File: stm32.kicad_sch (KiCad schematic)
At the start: 0 parts

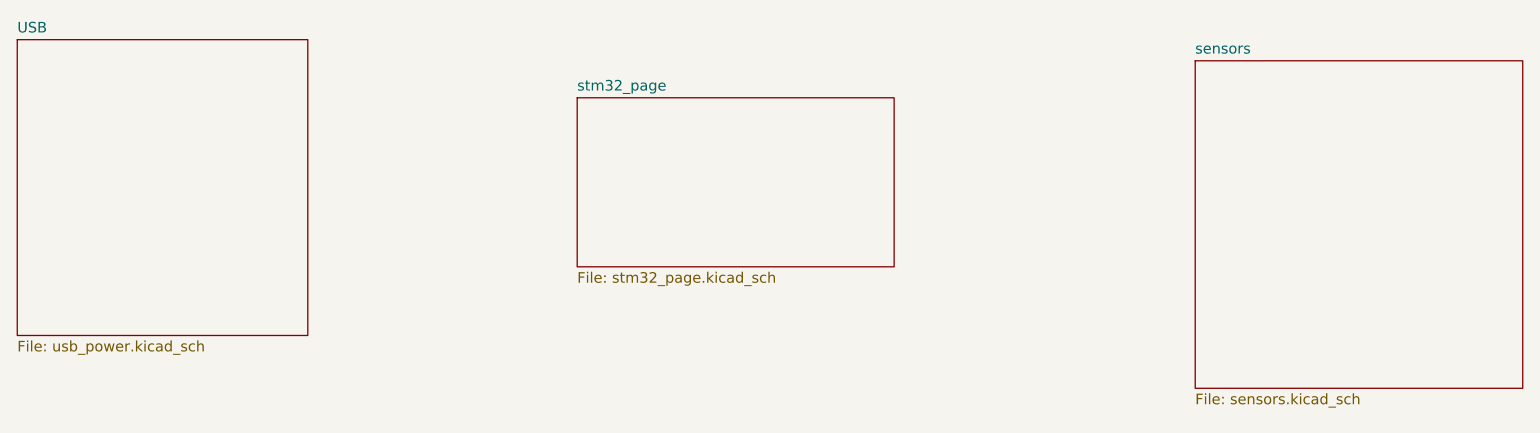
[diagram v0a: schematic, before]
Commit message: Finished schematic need to check , before layout
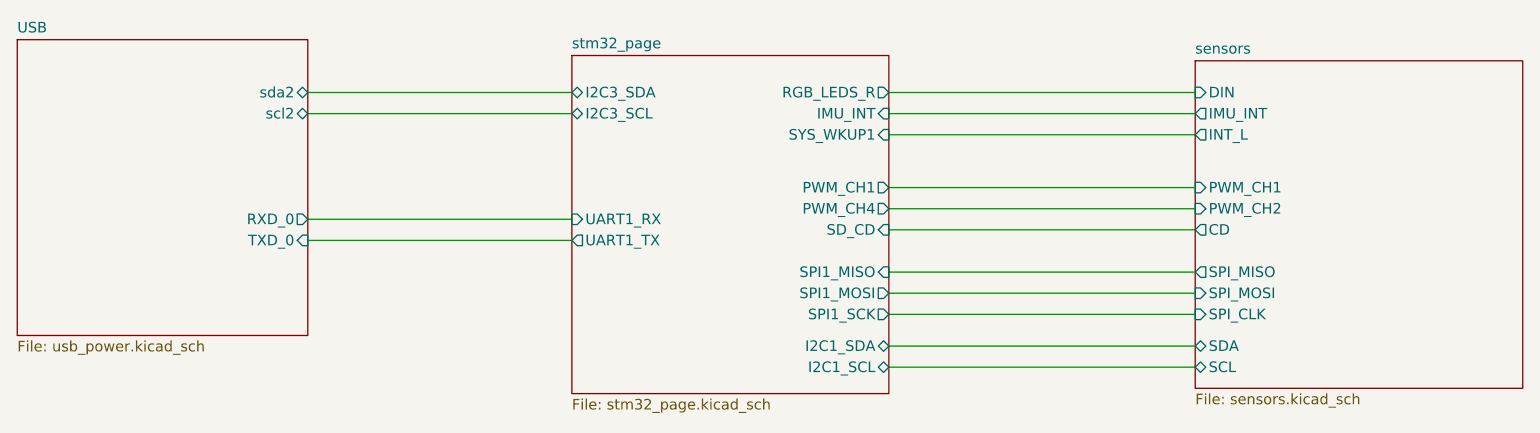
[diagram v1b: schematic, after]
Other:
- sheet USB ports: added RXD_0, TXD_0, scl2, sda2; removed none
- sheet sensors ports: added CD, DIN, IMU_INT, INT_L, PWM_CH1, PWM_CH2, SCL, SDA, SPI_CLK, SPI_MISO, SPI_MOSI; removed none
- sheet stm32_page ports: added I2C1_SCL, I2C1_SDA, I2C3_SCL, I2C3_SDA, IMU_INT, PWM_CH1, PWM_CH4, RGB_LEDS_R, SD_CD, SPI1_MISO, SPI1_MOSI, SPI1_SCK, SYS_WKUP1, UART1_RX, UART1_TX; removed none

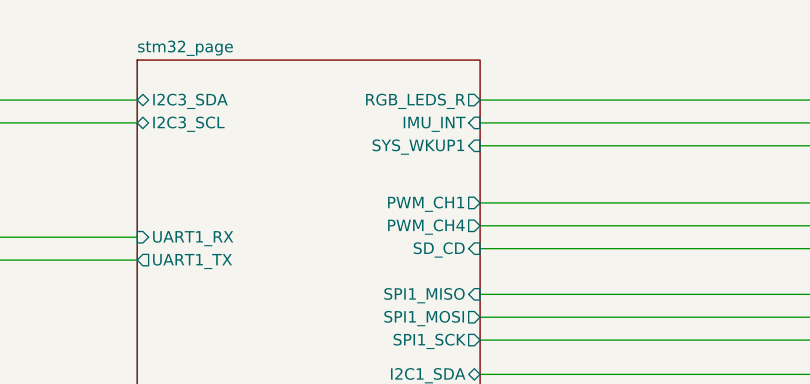
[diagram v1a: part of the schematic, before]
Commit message: Finished placement , added few TP's
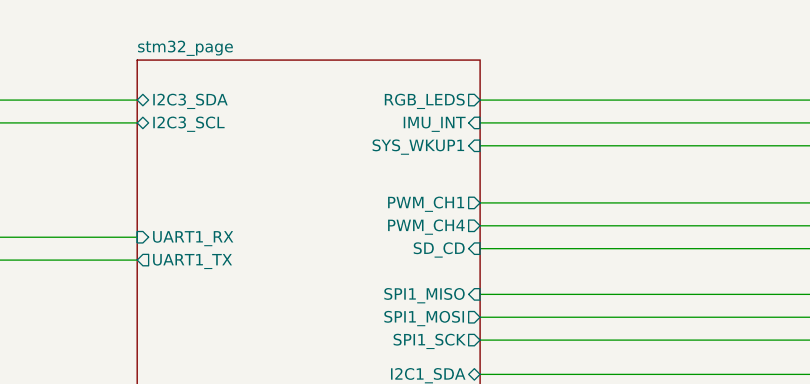
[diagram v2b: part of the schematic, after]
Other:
- sheet stm32_page ports: added RGB_LEDS; removed RGB_LEDS_R
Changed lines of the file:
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@@
-			)
-		)
-		(pin "RGB_LEDS_R" output
-			(at 157.48 43.18 0)
-			(effects
-				(font
-					(size 1.27 1.27)
-				)
-				(justify right)
 			)
 		)
@@
 			)
 		)
+		(pin "RGB_LEDS" output
+			(at 157.48 43.18 0)
+			(effects
+				(font
+					(size 1.27 1.27)
+				)
+				(justify right)
+			)
+		)
